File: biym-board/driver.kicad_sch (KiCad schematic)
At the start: 10 parts, among them J2 HEADER_01X03_JST_PH_VERTICAL, U1 DRV8311H

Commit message: output -> servo
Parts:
- removed J2: HEADER_01X03_JST_PH_VERTICAL, Janelia:JST_PH_B3B-PH-K_1x03_P2.00mm_Vertical, symbol Janelia:HEADER_01X03_JST_PH_VERTICAL
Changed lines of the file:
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@@
     (pin "2")
-  )
-  (symbol (lib_id "Janelia:HEADER_01X03_JST_PH_VERTICAL") (at 186.69 100.33 0) (unit 1)
-    (in_bom yes) (on_board yes)
-    (property "Reference" "J2" (id 0) (at 186.69 95.25 0))
-    (property "Value" "HEADER_01X03_JST_PH_VERTICAL" (id 1) (at 186.69 105.41 0))
-    (property "Footprint" "Janelia:JST_PH_B3B-PH-K_1x03_P2.00mm_Vertical" (id 2) (at 186.69 87.63 0)
-      (effects (font (size 1.27 1.27)) hide)
-    )
-    (property "Datasheet" "" (id 3) (at 186.69 100.33 0)
-      (effects (font (size 1.27 1.27)) hide)
-    )
-    (property "Description" "CONN HEADER VERT 3POS 2MM" (id 4) (at 186.69 90.17 0)
-      (effects (font (size 1.27 1.27)) hide)
-    )
-    (property "Manufacturer" "JST Sales America Inc." (id 5) (at 186.69 82.55 0)
-      (effects (font (size 1.27 1.27)) hide)
-    )
-    (property "Manufacturer Part Number" "B3B-PH-K-S(LF)(SN)" (id 6) (at 186.69 85.09 0)
-      (effects (font (size 1.27 1.27)) hide)
-    )
-    (property "Vendor" "Digi-Key" (id 7) (at 186.69 80.01 0)
-      (effects (font (size 1.27 1.27)) hide)
-    )
-    (property "Vendor Part Number" "455-1705-ND" (id 8) (at 186.69 77.47 0)
-      (effects (font (size 1.27 1.27)) hide)
-    )
-    (pin "1")
-    (pin "2")
-    (pin "3")
   )
   (symbol (lib_id "Janelia:0.1uF_0402") (at 212.09 55.88 0) (unit 1)

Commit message: Finished v0.1 of schematic
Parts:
- removed C1, C3, C4, C7: 0.1uF, Janelia:SM0402, symbol Janelia:0.1uF_0402
- removed C2, C5: 10uF, Janelia:SM0402_POL, symbol Janelia:10uF_0402_POL
- removed C6: 1uF, Janelia:SM0402_POL, symbol Janelia:1uF_0402_POL
- removed R2: 5.1k, Janelia:SM0402, symbol Janelia:5.1k_0402
- added C10, C4, C5, C8: C_0.1uF_0402, Janelia:SM0402, symbol Janelia:C_0.1uF_0402
- added C6, C7: C_10uF_0402_POL, Janelia:SM0402_POL, symbol Janelia:C_10uF_0402_POL
- added C9: C_1uF_0402_POL, Janelia:SM0402_POL, symbol Janelia:C_1uF_0402_POL
- added J2: HEADER_01X03_JST_ZH_SMD_VERTICAL, Janelia:JST_ZH_B3B_ZR_SM4_TF_1x03-1MP_P1.50mm_Vertical, symbol Janelia:HEADER_01X03_JST_ZH_SMD_VERTICAL
- added R2: R_5.1k_0402, Janelia:SM0402, symbol Janelia:R_5.1k_0402
- renumbered U1 to U2
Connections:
- net CP: now also C8.2
- net CSAREF: now also C10.1
- net GND: now also C10.2, C4.2, C5.2, C6.2, C7.2, C9.2
- net MOTOR_A: now also J2.1 (Pin_1)
- net MOTOR_B: now also J2.2 (Pin_2)
- net MOTOR_C: now also J2.3 (Pin_3)
- net VDD: now also C9.1
- net VDIGITAL: now also C5.1, C7.1, R2.1
- net VDRIVER: now also C4.1, C6.1, C8.1
- net ~{FAULT}: now also R2.2
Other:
- company: (none) -> Peter Polidoro
- title: biym-board-brushless-motor -> biym-board-driver

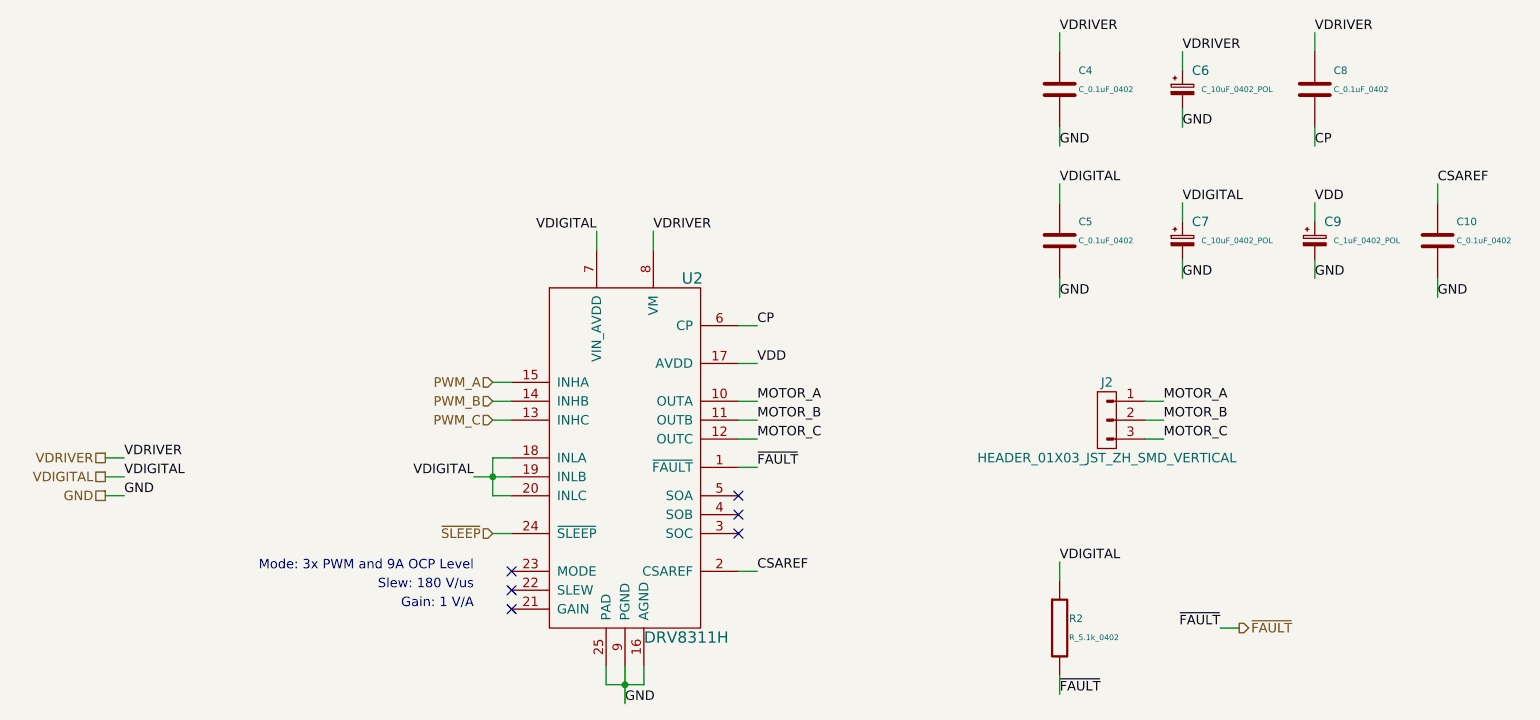
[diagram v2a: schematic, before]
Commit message: Add boost for both led and servo
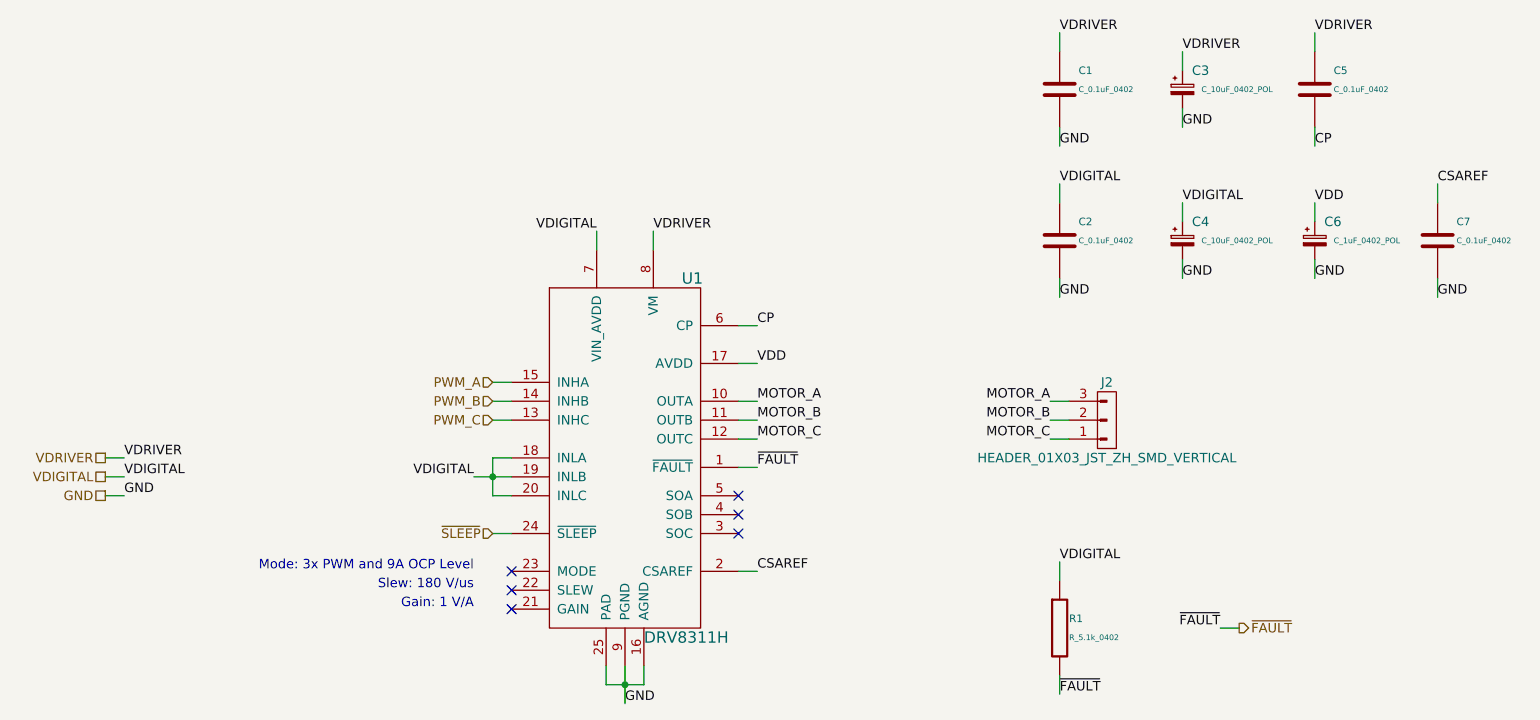
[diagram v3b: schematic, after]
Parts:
- renumbered C4 to C1, C5 to C2, C6 to C3, C7 to C4, C8 to C5, C9 to C6, C10 to C7, R2 to R1, U2 to U1
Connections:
- net MOTOR_A: now also J2.3 (Pin_3); no longer J2.1 (Pin_1)
- net MOTOR_C: now also J2.1 (Pin_1); no longer J2.3 (Pin_3)
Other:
- moved on the sheet: J2
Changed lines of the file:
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@@
     (stroke (width 0) (type default) (color 0 0 0 0))
   )
-  (wire (pts (xy 191.77 102.87) (xy 194.31 102.87))
+  (wire (pts (xy 181.61 97.79) (xy 179.07 97.79))
     (stroke (width 0) (type default) (color 0 0 0 0))
   )
@@
     (stroke (width 0) (type default) (color 0 0 0 0))
   )
-  (wire (pts (xy 191.77 100.33) (xy 194.31 100.33))
+  (wire (pts (xy 181.61 100.33) (xy 179.07 100.33))
     (stroke (width 0) (type default) (color 0 0 0 0))
   )
@@
     (stroke (width 0) (type default) (color 0 0 0 0))
   )
-  (wire (pts (xy 191.77 97.79) (xy 194.31 97.79))
+  (wire (pts (xy 181.61 102.87) (xy 179.07 102.87))
     (stroke (width 0) (type default) (color 0 0 0 0))
   )
@@
     (effects (font (size 1.27 1.27)) (justify left bottom))
   )
-  (label "MOTOR_C" (at 194.31 102.87 0)
-    (effects (font (size 1.27 1.27)) (justify left bottom))
-  )
-  (label "MOTOR_A" (at 194.31 97.79 0)
-    (effects (font (size 1.27 1.27)) (justify left bottom))
+  (label "MOTOR_C" (at 179.07 102.87 180)
+    (effects (font (size 1.27 1.27)) (justify right bottom))
+  )
+  (label "MOTOR_A" (at 179.07 97.79 180)
+    (effects (font (size 1.27 1.27)) (justify right bottom))
   )
   (label "VDRIVER" (at 180.34 48.26 0)
@@
     (effects (font (size 1.27 1.27)) (justify left bottom))
   )
-  (label "MOTOR_B" (at 194.31 100.33 0)
-    (effects (font (size 1.27 1.27)) (justify left bottom))
+  (label "MOTOR_B" (at 179.07 100.33 180)
+    (effects (font (size 1.27 1.27)) (justify right bottom))
   )
   (label "GND" (at 180.34 83.82 0)
@@
   (symbol (lib_id "Janelia:C_0.1uF_0402") (at 214.63 55.88 0) (unit 1)
     (in_bom yes) (on_board yes)
-    (property "Reference" "C8" (id 0) (at 217.17 53.34 0)
+    (property "Reference" "C5" (id 0) (at 217.17 53.34 0)
       (effects (font (size 1.016 1.016)) (justify left))
     )
@@
   (symbol (lib_id "Janelia:C_0.1uF_0402") (at 231.14 76.2 0) (unit 1)
     (in_bom yes) (on_board yes)
-    (property "Reference" "C10" (id 0) (at 233.68 73.66 0)
+    (property "Reference" "C7" (id 0) (at 233.68 73.66 0)
       (effects (font (size 1.016 1.016)) (justify left))
     )
@@
   (symbol (lib_id "Janelia:C_0.1uF_0402") (at 180.34 55.88 0) (unit 1)
     (in_bom yes) (on_board yes)
-    (property "Reference" "C4" (id 0) (at 182.88 53.34 0)
+    (property "Reference" "C1" (id 0) (at 182.88 53.34 0)
       (effects (font (size 1.016 1.016)) (justify left))
     )
@@
   (symbol (lib_id "Janelia:C_1uF_0402_POL") (at 214.63 76.2 0) (unit 1)
     (in_bom yes) (on_board yes)
-    (property "Reference" "C9" (id 0) (at 215.9 73.66 0)
+    (property "Reference" "C6" (id 0) (at 215.9 73.66 0)
       (effects (font (size 1.27 1.27)) (justify left))
     )
@@
   (symbol (lib_id "Janelia:C_0.1uF_0402") (at 180.34 76.2 0) (unit 1)
     (in_bom yes) (on_board yes)
-    (property "Reference" "C5" (id 0) (at 182.88 73.66 0)
+    (property "Reference" "C2" (id 0) (at 182.88 73.66 0)
       (effects (font (size 1.016 1.016)) (justify left))
     )
@@
   (symbol (lib_id "Janelia:R_5.1k_0402") (at 180.34 128.27 0) (unit 1)
     (in_bom yes) (on_board yes)
-    (property "Reference" "R2" (id 0) (at 181.61 127 0)
+    (property "Reference" "R1" (id 0) (at 181.61 127 0)
       (effects (font (size 1.016 1.016)) (justify left))
     )
@@
   (symbol (lib_id "Janelia:DRV8311H") (at 121.92 105.41 0) (unit 1)
     (in_bom yes) (on_board yes)
-    (property "Reference" "U2" (id 0) (at 129.54 81.28 0)
+    (property "Reference" "U1" (id 0) (at 129.54 81.28 0)
       (effects (font (size 1.524 1.524)) (justify left))
     )
@@
   (symbol (lib_id "Janelia:C_10uF_0402_POL") (at 196.85 55.88 0) (unit 1)
     (in_bom yes) (on_board yes)
-    (property "Reference" "C6" (id 0) (at 198.12 53.34 0)
+    (property "Reference" "C3" (id 0) (at 198.12 53.34 0)
       (effects (font (size 1.27 1.27)) (justify left))
     )
@@
     (pin "2")
   )
-  (symbol (lib_id "Janelia:HEADER_01X03_JST_ZH_SMD_VERTICAL") (at 186.69 100.33 0) (unit 1)
+  (symbol (lib_id "Janelia:HEADER_01X03_JST_ZH_SMD_VERTICAL") (at 186.69 100.33 180) (unit 1)
     (in_bom yes) (on_board yes)
     (property "Reference" "J2" (id 0) (at 186.69 95.25 0))
     (property "Value" "HEADER_01X03_JST_ZH_SMD_VERTICAL" (id 1) (at 186.69 105.41 0))
-    (property "Footprint" "Janelia:JST_ZH_B3B_ZR_SM4_TF_1x03-1MP_P1.50mm_Vertical" (id 2) (at 186.69 87.63 0)
+    (property "Footprint" "Janelia:JST_ZH_B3B_ZR_SM4_TF_1x03-1MP_P1.50mm_Vertical" (id 2) (at 186.69 113.03 0)
       (effects (font (size 1.27 1.27)) hide)
     )
@@
       (effects (font (size 1.27 1.27)) hide)
     )
-    (property "Description" "CONN HEADER SMD 3POS 1.5MM" (id 4) (at 186.69 90.17 0)
-      (effects (font (size 1.27 1.27)) hide)
-    )
-    (property "Manufacturer" "JST Sales America Inc." (id 5) (at 186.69 82.55 0)
-      (effects (font (size 1.27 1.27)) hide)
-    )
-    (property "Manufacturer Part Number" "B3B-ZR-SM4-TF(LF)(SN)" (id 6) (at 186.69 85.09 0)
-      (effects (font (size 1.27 1.27)) hide)
-    )
-    (property "Vendor" "Digi-Key" (id 7) (at 186.69 80.01 0)
-      (effects (font (size 1.27 1.27)) hide)
-    )
-    (property "Vendor Part Number" "B3B-ZR-SM4-TF(LF)(SN)" (id 8) (at 186.69 77.47 0)
+    (property "Description" "CONN HEADER SMD 3POS 1.5MM" (id 4) (at 186.69 110.49 0)
+      (effects (font (size 1.27 1.27)) hide)
+    )
+    (property "Manufacturer" "JST Sales America Inc." (id 5) (at 186.69 118.11 0)
+      (effects (font (size 1.27 1.27)) hide)
+    )
+    (property "Manufacturer Part Number" "B3B-ZR-SM4-TF(LF)(SN)" (id 6) (at 186.69 115.57 0)
+      (effects (font (size 1.27 1.27)) hide)
+    )
+    (property "Vendor" "Digi-Key" (id 7) (at 186.69 120.65 0)
+      (effects (font (size 1.27 1.27)) hide)
+    )
+    (property "Vendor Part Number" "B3B-ZR-SM4-TF(LF)(SN)" (id 8) (at 186.69 123.19 0)
       (effects (font (size 1.27 1.27)) hide)
     )
@@
   (symbol (lib_id "Janelia:C_10uF_0402_POL") (at 196.85 76.2 0) (unit 1)
     (in_bom yes) (on_board yes)
-    (property "Reference" "C7" (id 0) (at 198.12 73.66 0)
+    (property "Reference" "C4" (id 0) (at 198.12 73.66 0)
       (effects (font (size 1.27 1.27)) (justify left))
     )

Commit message: Completed v1.1 layout
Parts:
- C1, C2, C5, C7: value C_0.1uF_0402 -> 0.1uF
- C3, C4: value C_10uF_0402_POL -> 10uF
- C6: value C_1uF_0402_POL -> 1uF
- R1: value R_5.1k_0402 -> 5.1k
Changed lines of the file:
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@@
   (title_block
     (title "biym-board-driver")
-    (date "2022-11-17")
-    (rev "1.0")
+    (date "2022-11-20")
+    (rev "1.1")
     (company "Peter Polidoro")
   )
@@
       (effects (font (size 1.016 1.016)) (justify left))
     )
-    (property "Value" "C_0.1uF_0402" (id 1) (at 217.17 55.88 0)
+    (property "Value" "0.1uF" (id 1) (at 217.17 55.88 0)
       (effects (font (size 0.762 0.762)) (justify left))
     )
@@
       (effects (font (size 1.016 1.016)) (justify left))
     )
-    (property "Value" "C_0.1uF_0402" (id 1) (at 233.68 76.2 0)
+    (property "Value" "0.1uF" (id 1) (at 233.68 76.2 0)
       (effects (font (size 0.762 0.762)) (justify left))
     )
@@
       (effects (font (size 1.016 1.016)) (justify left))
     )
-    (property "Value" "C_0.1uF_0402" (id 1) (at 182.88 55.88 0)
+    (property "Value" "0.1uF" (id 1) (at 182.88 55.88 0)
       (effects (font (size 0.762 0.762)) (justify left))
     )
@@
       (effects (font (size 1.27 1.27)) (justify left))
     )
-    (property "Value" "C_1uF_0402_POL" (id 1) (at 217.17 76.2 0)
+    (property "Value" "1uF" (id 1) (at 217.17 76.2 0)
       (effects (font (size 0.762 0.762)) (justify left))
     )
@@
       (effects (font (size 1.016 1.016)) (justify left))
     )
-    (property "Value" "C_0.1uF_0402" (id 1) (at 182.88 76.2 0)
+    (property "Value" "0.1uF" (id 1) (at 182.88 76.2 0)
       (effects (font (size 0.762 0.762)) (justify left))
     )
@@
       (effects (font (size 1.016 1.016)) (justify left))
     )
-    (property "Value" "R_5.1k_0402" (id 1) (at 181.61 129.54 0)
+    (property "Value" "5.1k" (id 1) (at 181.61 129.54 0)
       (effects (font (size 0.762 0.762)) (justify left))
     )
@@
       (effects (font (size 1.27 1.27)) (justify left))
     )
-    (property "Value" "C_10uF_0402_POL" (id 1) (at 199.39 55.88 0)
+    (property "Value" "10uF" (id 1) (at 199.39 55.88 0)
       (effects (font (size 0.762 0.762)) (justify left))
     )
@@
       (effects (font (size 1.27 1.27)) (justify left))
     )
-    (property "Value" "C_10uF_0402_POL" (id 1) (at 199.39 76.2 0)
-      (effects (font (size 0.762 0.762)) (justify left))
-    )
+    (property "Value" "10uF" (id 1) (at 199.39 76.2 0)
+      (effects (font (size 0.762 0.762)) (justify left))
+    )

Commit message: Update to kicad 7
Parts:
- U1: LCSC (none) -> C5218862; Package (none) -> WQFN-24(3x3); Synopsis (none) -> 24V ABS MAX 3 TO 20V 3-PHASE B
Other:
- title: biym-board-driver -> biym-board
